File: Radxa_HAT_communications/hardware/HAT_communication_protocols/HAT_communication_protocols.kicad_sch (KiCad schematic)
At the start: 66 parts, among them J1 Conn_01x02_Pin, J2 Can_terminals, J3 120Can-resistor, J4 Power_supply_12V, J5 LoRa_DIO, Q1 NMOS, U1 AMS1117-5.0, U2 LD1117V33, U3 74HC04, U4 MAX3485, U5 MCP2515-xSO, U6 TJA1051T-3, Y1 8MHz

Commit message: new docummentation
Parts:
- removed C1: 100nf, symbol Device:C_Small
- removed C15: 100nf, Resistor_SMD:R_0603_1608Metric_Pad0.98x0.95mm_HandSolder, symbol Device:C_Small
- removed C3: x, symbol Device:C_Small
- removed L1: FerriteBead_0603_1.5A, 4ms_Resistor:R_0603, symbol PCM_4ms_Inductor:FerriteBead_0603_1.5A
- added C18: 1uf, Resistor_SMD:R_0603_1608Metric_Pad0.98x0.95mm_HandSolder, symbol Device:C_Small
- added C19: 10uf, Resistor_SMD:R_0603_1608Metric_Pad0.98x0.95mm_HandSolder, symbol Device:C_Small
- added C3: x, symbol Device:C_US
- added L1: L_Ferrite, symbol Device:L_Ferrite
- added U7: LD1117V33, Package_TO_SOT_SMD:SOT-223-3_TabPin2, symbol Regulator_Linear:LD1117V33
- 2-Pin_Power_input1: footprint 4ms_Connector:Pins_1x02_2.54mm_TH -> Connector_PinHeader_2.54mm:PinHeader_1x02_P2.54mm_Vertical
- C17, R4, R9: footprint (none) -> Resistor_SMD:R_0603_1608Metric_Pad0.98x0.95mm_HandSolder
- R2, R3: value 1K8 -> 2k4
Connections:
- net GPIO03 is gone; now on net CAN_SI: RadxaGPIO1.15 (Pin_15)
- net GPIO04 is gone; now on net CAN_SO: RadxaGPIO1.7 (Pin_7)
- net GPIO05 is gone; now on net CAN_CS: RadxaGPIO1.11 (Pin_11)
- net GPIO06 is gone; now on net CAN_SCK: RadxaGPIO1.13 (Pin_13)
- net RXD is gone; now on net GPIO21: U3.4, U3.5
- net TXD is gone; now on net GPIO20: R5.2, U3.1
- net 12V: now also C3.1, L1.2; no longer C4.1, C5.1, U1.3 (VI), U2.3 (VI)
- net GND: now also C18.2, C19.2, C3.2, U7.1 (GND)
- net PS+3.3v: no longer C16.1, SX1.13 (3.3V)
- net PS+5v: no longer U6.5 (VIO)
- net at D6.1 (A1), D7.2 (A2), F3.2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: now also R9.2
- net at D5.1 (A1), D6.2 (A2), F2.1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: now also J1.1 (Pin_1)
- net at C2.1, D10.1 (K), D3.2 (A2)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: now also L1.1
- net at F3.1, RS485_interface1.2 (Pin_2): no longer R9.2
- net at F2.2, RS485_interface1.1 (Pin_1): no longer J1.1 (Pin_1)
- new net: C4.1, U2.3 (VI)
- new net: C19.1, U7.3 (VI)
- new net: C5.1, U1.3 (VI)
- new net LoRa+3.3v: C16.1, C18.1, SX1.13 (3.3V), U7.2 (VO)
- no-connect marks 6 -> 7
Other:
- note added: "2.2mA MAX"
- note added: "80mA MAX"
- note added: "Transmit (TX) Current: 650 mA (maximum, at 30 dBm output power)"
- moved on the sheet: 2-Pin_Power_input1, C10, C11, C12, C13, C14, C17, C2, C4, C5, C6, C7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

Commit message: PCB design | PCB countors finally drew and correct placement of pinheaders and pin socker so they fit to the Radxa-X4 form factor
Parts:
- added J6: PoE, Connector_PinSocket_2.54mm:PinSocket_2x02_P2.54mm_Vertical, symbol Connector_Generic:Conn_02x02_Top_Bottom
- 2-Pin_Power_input1: footprint Connector_PinHeader_2.54mm:PinHeader_1x02_P2.54mm_Vertical -> Connector_PinSocket_2.54mm:PinSocket_1x02_P2.54mm_Vertical
- J2, J4: footprint TerminalBlock:TerminalBlock_Xinya_XY308-2.54-2P_1x02_P2.54mm_Horizontal -> TerminalBlock_MetzConnect:TerminalBlock_MetzConnect_Type101_RT01602HBWC_1x02_P5.08mm_Horizontal
- RS485_interface1: footprint TerminalBlock:TerminalBlock_Xinya_XY308-2.54-3P_1x03_P2.54mm_Horizontal -> TerminalBlock_CUI:TerminalBlock_CUI_TB007-508-03_1x03_P5.08mm_Horizontal
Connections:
- new net vc1: J6.2 (Pin_2)
- new net vc2: J6.1 (Pin_1)
- new net vc3: J6.4 (Pin_4)
- new net vc4: J6.3 (Pin_3)
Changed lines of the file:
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@@
 	(wire
 		(pts
+			(xy 388.62 102.87) (xy 387.35 102.87)
+		)
+		(stroke
+			(width 0)
+			(type default)
+		)
+	)
+	(wire
+		(pts
 			(xy 78.74 54.61) (xy 78.74 62.23)
 		)
@@
 	(wire
 		(pts
+			(xy 388.62 100.33) (xy 387.35 100.33)
+		)
+		(stroke
+			(width 0)
+			(type default)
+		)
+	)
+	(wire
+		(pts
 			(xy 215.9 152.4) (xy 213.36 152.4)
 		)
@@
 	(wire
 		(pts
+			(xy 402.59 102.87) (xy 401.32 102.87)
+		)
+		(stroke
+			(width 0)
+			(type default)
+		)
+	)
+	(wire
+		(pts
 			(xy 146.05 154.94) (xy 146.05 147.32)
 		)
@@
 	(wire
 		(pts
+			(xy 402.59 100.33) (xy 401.32 100.33)
+		)
+		(stroke
+			(width 0)
+			(type default)
+		)
+	)
+	(wire
+		(pts
 			(xy 125.73 124.46) (xy 125.73 127)
 		)
@@
 		)
 	)
+	(label "vc4"
+		(at 402.59 100.33 0)
+		(effects
+			(font
+				(size 1.27 1.27)
+			)
+			(justify left bottom)
+		)
+	)
 	(label "GPIO25"
 		(at 215.9 175.26 0)
@@
 		)
 	)
+	(label "vc1"
+		(at 387.35 102.87 180)
+		(effects
+			(font
+				(size 1.27 1.27)
+			)
+			(justify right bottom)
+		)
+	)
 	(label "GPIO06"
 		(at 304.8 152.4 0)
@@
 		)
 	)
+	(label "vc2"
+		(at 387.35 100.33 180)
+		(effects
+			(font
+				(size 1.27 1.27)
+			)
+			(justify right bottom)
+		)
+	)
 	(label "LoRa_D1"
 		(at 224.79 33.02 0)
@@
 		)
 	)
+	(label "vc3"
+		(at 402.59 102.87 0)
+		(effects
+			(font
+				(size 1.27 1.27)
+			)
+			(justify left bottom)
+		)
+	)
 	(label "GPIO03"
 		(at 198.12 144.78 180)
@@
 			)
 		)
-		(property "Footprint" "Connector_PinHeader_2.54mm:PinHeader_1x02_P2.54mm_Vertical"
+		(property "Footprint" "Connector_PinSocket_2.54mm:PinSocket_1x02_P2.54mm_Vertical"
 			(at 396.875 23.495 0)
 			(effects
@@
 	)
 	(symbol
+		(lib_id "Connector_Generic:Conn_02x02_Top_Bottom")
+		(at 393.7 100.33 0)
+		(unit 1)
+		(exclude_from_sim no)
+		(in_bom yes)
+		(on_board yes)
+		(dnp no)
+		(property "Reference" "J6"
+			(at 394.97 93.98 0)
+			(effects
+				(font
+					(size 1.27 1.27)
+				)
+			)
+		)
+		(property "Value" "PoE"
+			(at 394.97 96.52 0)
+			(effects
+				(font
+					(size 1.27 1.27)
+				)
+			)
+		)
+		(property "Footprint" "Connector_PinSocket_2.54mm:PinSocket_2x02_P2.54mm_Vertical"
+			(at 393.7 100.33 0)
+			(effects
+				(font
+					(size 1.27 1.27)
+				)
+				(hide yes)
+			)
+		)
+		(property "Datasheet" "~"
+			(at 393.7 100.33 0)
+			(effects
+				(font
+					(size 1.27 1.27)
+				)
+				(hide yes)
+			)
+		)
+		(property "Description" "Generic connector, double row, 02x02, top/bottom pin numbering scheme (row 1: 1...pins_per_row, row2: pins_per_row+1 ... num_pins), script generated (kicad-library-utils/schlib/autogen/connector/)"
+			(at 393.7 100.33 0)
+			(effects
+				(font
+					(size 1.27 1.27)
+				)
+				(hide yes)
+			)
+		)
+		(pin "2"
+		)
+		(pin "4"
+		)
+		(pin "1"
+		)
+		(pin "3"
+		)
+		(instances
+			(project ""
+				(path "/c2c24d05-340c-4010-9daf-2c9fe65e9278"
+					(reference "J6")
+					(unit 1)
+				)
+			)
+		)
+	)
+	(symbol
 		(lib_id "power:GND")
 		(at 78.74 76.2 0)
@@
 			)
 		)
-		(property "Footprint" "TerminalBlock:TerminalBlock_Xinya_XY308-2.54-2P_1x02_P2.54mm_Horizontal"
+		(property "Footprint" "TerminalBlock_MetzConnect:TerminalBlock_MetzConnect_Type101_RT01602HBWC_1x02_P5.08mm_Horizontal"
 			(at 304.8 30.48 0)
 			(effects
@@
 			)
 		)
-		(property "Footprint" "TerminalBlock:TerminalBlock_Xinya_XY308-2.54-2P_1x02_P2.54mm_Horizontal"
+		(property "Footprint" "TerminalBlock_MetzConnect:TerminalBlock_MetzConnect_Type101_RT01602HBWC_1x02_P5.08mm_Horizontal"
 			(at 154.94 134.62 0)
 			(effects
@@
 			)
 		)
-		(property "Footprint" "TerminalBlock:TerminalBlock_Xinya_XY308-2.54-3P_1x03_P2.54mm_Horizontal"
+		(property "Footprint" "TerminalBlock_CUI:TerminalBlock_CUI_TB007-508-03_1x03_P5.08mm_Horizontal"
 			(at 152.4 35.56 0)
 			(effects

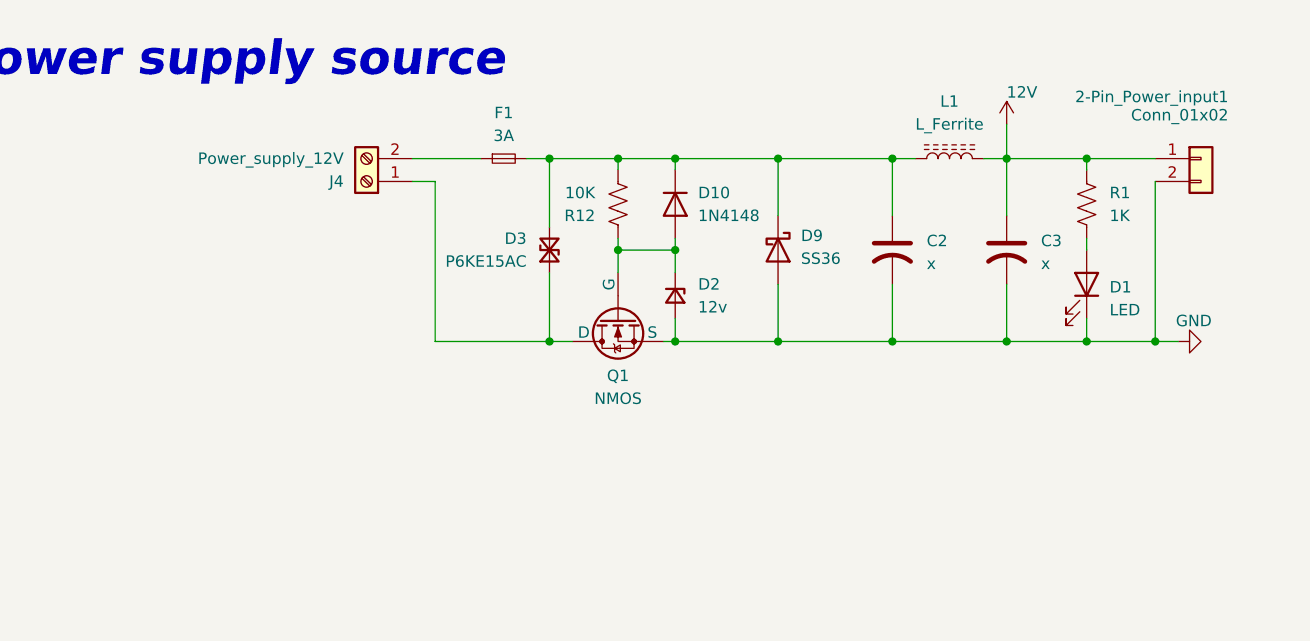
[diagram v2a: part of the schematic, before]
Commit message: Placement of some components in PCB layout. Thinking on adding a buck converter
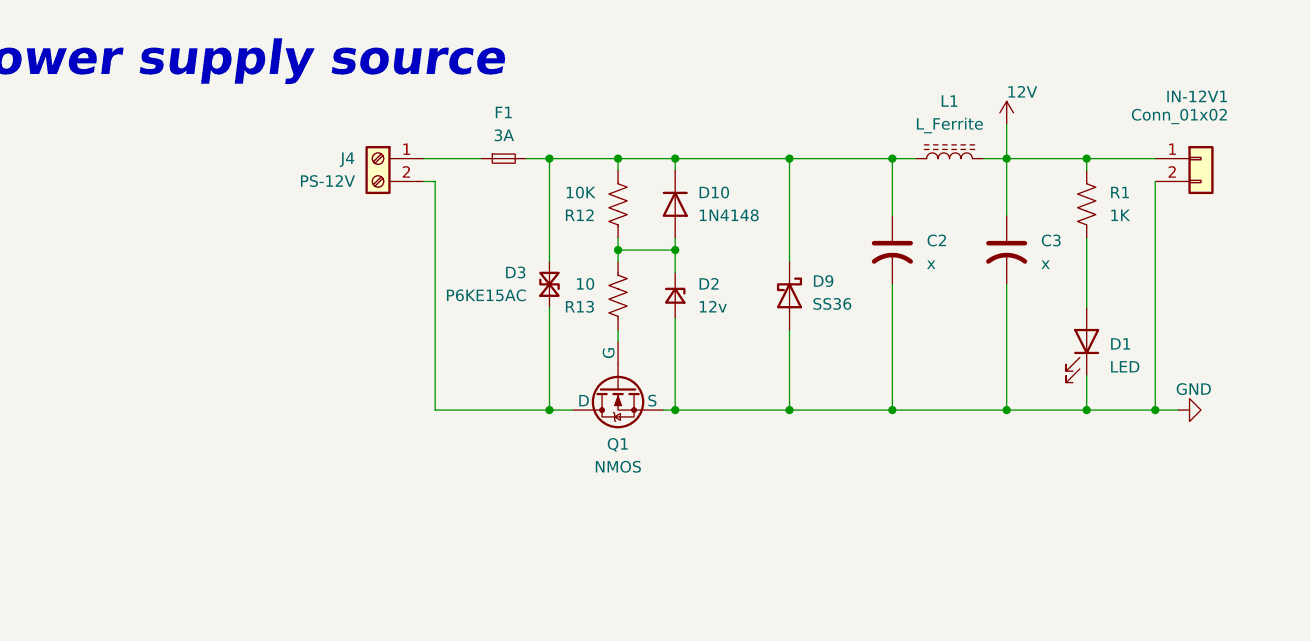
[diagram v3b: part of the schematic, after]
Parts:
- added R13: 10, Resistor_SMD:R_0603_1608Metric_Pad0.98x0.95mm_HandSolder, symbol Device:R_US
- J4: value Power_supply_12V -> PS-12V
- RS485_interface1: footprint TerminalBlock_CUI:TerminalBlock_CUI_TB007-508-03_1x03_P5.08mm_Horizontal -> TerminalBlock_MetzConnect:TerminalBlock_MetzConnect_Type101_RT01603HBWC_1x03_P5.08mm_Horizontal
- renumbered 2-Pin_Power_input1 to IN-12V1
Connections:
- net at D10.2 (A), D2.1 (K), R12.1: now also R13.2; no longer Q1.1 (G)
- net at F1.1: now also J4.1 (Pin_1); no longer J4.2 (Pin_2)
- net at D3.1 (A1), Q1.2 (D): now also J4.2 (Pin_2); no longer J4.1 (Pin_1)
- new net: Q1.1 (G), R13.1
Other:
- moved on the sheet: D1, D3, D9, J4, Q1

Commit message: PCB layout first version done
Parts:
- removed C2, C3: x, symbol Device:C_US
- removed D10: 1N4148, Diode_THT:D_DO-35_SOD27_P7.62mm_Horizontal, symbol Diode:1N4148
- removed L1: L_Ferrite, symbol Device:L_Ferrite
- removed U2: LD1117V33, Package_TO_SOT_SMD:SOT-223-3_TabPin2, symbol Regulator_Linear:LD1117V33
- added C1: 10uF /25v, Capacitor_SMD:C_1206_3216Metric_Pad1.33x1.80mm_HandSolder, symbol Device:C_US
- added C15: 10nf, Resistor_SMD:R_0603_1608Metric_Pad0.98x0.95mm_HandSolder, symbol Device:C_Small
- added C3: 22uF 6.3v, Capacitor_SMD:C_1206_3216Metric_Pad1.33x1.80mm_HandSolder, symbol Device:C_Small
- added D8: 1N4148W, Diode_SMD:D_SOD-123, symbol Diode:1N4148W
- added L2: 100uH_1.0A, Inductor_SMD:L_Wuerth_WE-PD-Typ-M-Typ-S_Handsoldering, symbol PCM_4ms_Inductor:10uH_1.0A_4018
- added R14: 100K, Resistor_SMD:R_0603_1608Metric_Pad0.98x0.95mm_HandSolder, symbol Device:R_US
- added R15: 6k8, Resistor_SMD:R_0603_1608Metric_Pad0.98x0.95mm_HandSolder, symbol Device:R_US
- added R16, R17: 10k, Resistor_SMD:R_0603_1608Metric_Pad0.98x0.95mm_HandSolder, symbol Device:R_US
- added U2: MP2307, Package_SO:SOIC-8-1EP_3.9x4.9mm_P1.27mm_EP2.62x3.51mm, symbol Regulator_Switching:MP2303ADN
- AE1: footprint (none) -> Connector_PinHeader_2.54mm:PinHeader_1x01_P2.54mm_Vertical
- C4: value 10uf -> 100nf
- C7: value 1uf -> 3.9nf
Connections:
- net LoRa+3.3v is gone; now on net PS+3.3v: C16.1, C18.1, SX1.13 (3.3V), U7.2 (VO)
- net 12V: now also D3.2 (A2), D9.1 (K), F1.2, R12.2, C1.1, D8.1 (K), R14.1, U2.2 (IN); no longer R1.1
- net COMs: now also RS485_interface1.1 (Pin_1); no longer RS485_interface1.3 (Pin_3)
- net GND: now also C1.2, C3.2, R15.2, R16.2, U2.4 (GND); no longer C7.2
- net PS+3.3v: no longer C7.1
- net PS+5v: now also C19.1, U7.3 (VI)
- net at R10.1, U6.6 (CANL): now also J2.1 (Pin_1); no longer J2.2 (Pin_2)
- net at J3.2 (Pin_2), U6.7 (CANH): now also J2.2 (Pin_2); no longer J2.1 (Pin_1)
- net at D2.1 (K), R12.1, R13.2: now also D8.2 (A)
- net at C4.1: now also U2.8 (SS)
- net at F2.2: now also RS485_interface1.3 (Pin_3); no longer RS485_interface1.1 (Pin_1)
- net PS+6.2v: now reaches C5.1, U1.3 (VI)
- net PS+6.2v: now also R1.1, C3.1, L2.2, R17.1
- new net: C7.2, R15.1
- new net: C7.1, U2.6 (COMP)
- new net: C15.2, L2.1, U2.3 (SW)
- new net: R16.1, R17.2, U2.5 (FB)
- new net: C15.1, U2.1 (BS)
- new net: R14.2, U2.7 (EN)
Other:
- note added: "Transmit (TX) Current: 120 mA (maximum, at +20 dBm output power)"
- note removed: "2.2mA MAX"
- note removed: "80mA MAX"
- note removed: "Transmit (TX) Current: 650 mA (maximum, at 30 dBm output power)"
- moved on the sheet: C8, D1, D2, D3, D9, F1, IN-12V1, J4, J6, Q1, R1, R12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

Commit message: PCB tracks 60% completed
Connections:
- net LoRa_D1: now also J5.3 (Pin_3); no longer J5.2 (Pin_2)
- net LoRa_D2: now also J5.2 (Pin_2); no longer J5.3 (Pin_3)
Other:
- moved on the sheet: C4
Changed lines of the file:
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@@
 	(wire
 		(pts
-			(xy 321.31 48.26) (xy 321.31 43.18)
+			(xy 321.31 53.34) (xy 321.31 43.18)
 		)
 		(stroke
@@
 	(wire
 		(pts
-			(xy 321.31 53.34) (xy 321.31 68.58)
+			(xy 321.31 58.42) (xy 321.31 68.58)
 		)
 		(stroke
@@
 	)
 	(image
-		(at 292.1 -26.67)
+		(at 342.9 -25.4)
 		(data "iVBORw0KGgoAAAANSUhEUgAAAyAAAAMgCAIAAABUEpE/AAAAA3NCSVQICAjb4U/gAAAgAElEQVR4"
 			"nOzdeZhU5Zk+/vfstXdVV1V3NU0D3SwiioBEdllkJCqCgtGYqKMmZtG4JJNkdDT5GicuuIwRiSYO"
@@
 		)
 	)
-	(label "LoRa_D2"
-		(at 233.68 90.17 180)
-		(effects
-			(font
-				(size 1.27 1.27)
-			)
-			(justify right bottom)
-		)
-	)
 	(label "SPI0_Tx"
 		(at 266.7 137.16 0)
@@
 		)
 	)
+	(label "LoRa_D2"
+		(at 233.68 92.71 180)
+		(effects
+			(font
+				(size 1.27 1.27)
+			)
+			(justify right bottom)
+		)
+	)
 	(label "COMs"
 		(at 116.84 60.96 0)
@@
 		)
 	)
-	(label "LoRa_D1"
-		(at 233.68 92.71 180)
-		(effects
-			(font
-				(size 1.27 1.27)
-			)
-			(justify right bottom)
-		)
-	)
 	(label "SPI0_NSS"
 		(at 304.8 143.51 0)
@@
 		)
 	)
+	(label "LoRa_D1"
+		(at 233.68 90.17 180)
+		(effects
+			(font
+				(size 1.27 1.27)
+			)
+			(justify right bottom)
+		)
+	)
 	(label "GPIO26"
 		(at 215.9 170.18 0)
@@
 		(lib_id "Device:C_Small")
 		(at 330.2 55.88 0)
-		(mirror y)
 		(unit 1)
 		(exclude_from_sim no)
@@
 		(dnp no)
 		(property "Reference" "C7"
-			(at 332.74 55.88 0)
+			(at 327.66 55.88 0)
 			(effects
 				(font
@@
 		)
 		(property "Value" "3.9nf"
-			(at 332.74 53.34 0)
+			(at 327.66 53.34 0)
 			(effects
 				(font
@@
 		(dnp no)
 		(property "Reference" "J6"
-			(at 307.848 86.36 0)
+			(at 309.88 86.36 0)
 			(effects
 				(font
@@
 		)
 		(property "Value" "PoE"
-			(at 311.15 86.36 0)
+			(at 313.182 86.36 0)
 			(effects
 				(font
@@
 	(symbol
 		(lib_id "Device:C_Small")
-		(at 321.31 50.8 0)
-		(mirror y)
+		(at 321.31 55.88 0)
 		(unit 1)
 		(exclude_from_sim no)
@@
 		(dnp no)
 		(property "Reference" "C4"
-			(at 323.85 50.8 0)
+			(at 318.77 55.88 0)
 			(effects
 				(font
@@
 		)
 		(property "Value" "100nf"
-			(at 323.85 48.26 0)
+			(at 318.77 53.34 0)
 			(effects
 				(font
@@
 		)
 		(property "Footprint" "Resistor_SMD:R_0603_1608Metric_Pad0.98x0.95mm_HandSolder"
-			(at 321.31 50.8 0)
+			(at 321.31 55.88 0)
 			(effects
 				(font
@@
 		)
 		(property "Datasheet" "~"
-			(at 321.31 50.8 0)
+			(at 321.31 55.88 0)
 			(effects
 				(font
@@
 		)
 		(property "Description" "Unpolarized capacitor, small symbol"
-			(at 321.31 50.8 0)
+			(at 321.31 55.88 0)
 			(effects
 				(font

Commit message: PCB V1 done
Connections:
- net 3.3v_gpio renamed 3.3v_pin1
- net 3.3v_pin1: no longer RadxaGPIO1.17 (Pin_17)
- net 5v_gpio renamed 5v_pin2
- net 5v_pin2: no longer RadxaGPIO1.4 (Pin_4)
- new net 3.3v_pin17: RadxaGPIO1.17 (Pin_17)
- new net 5v_pin4: RadxaGPIO1.4 (Pin_4)
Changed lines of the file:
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@@
 	)
 	(junction
-		(at 214.63 127)
-		(diameter 0)
-		(color 0 0 0 0)
-	)
-	(junction
 		(at 34.29 151.13)
 		(diameter 0)
@@
 	(wire
 		(pts
-			(xy 213.36 129.54) (xy 214.63 129.54)
+			(xy 213.36 129.54) (xy 222.25 129.54)
 		)
 		(stroke
@@
 	(wire
 		(pts
-			(xy 222.25 127) (xy 214.63 127)
-		)
-		(stroke
-			(width 0)
-			(type default)
-		)
-	)
-	(wire
-		(pts
 			(xy 21.59 52.07) (xy 21.59 55.88)
 		)
@@
 	(wire
 		(pts
-			(xy 214.63 129.54) (xy 214.63 127)
-		)
-		(stroke
-			(width 0)
-			(type default)
-		)
-	)
-	(wire
-		(pts
 			(xy 215.9 165.1) (xy 213.36 165.1)
 		)
@@
 	(wire
 		(pts
-			(xy 214.63 127) (xy 213.36 127)
-		)
-		(stroke
-			(width 0)
-			(type default)
-		)
-	)
-	(wire
-		(pts
 			(xy 236.22 44.45) (xy 236.22 45.72)
 		)
@@
 	(wire
 		(pts
+			(xy 213.36 127) (xy 222.25 127)
+		)
+		(stroke
+			(width 0)
+			(type default)
+		)
+	)
+	(wire
+		(pts
 			(xy 365.76 48.26) (xy 363.22 48.26)
 		)
@@
 			)
 		)
-		(property "Value" "5v_gpio"
+		(property "Value" "5v_pin2"
 			(at 225.552 127 90)
 			(effects
@@
 		(lib_id "Device:R_US")
 		(at 106.68 27.94 0)
+		(mirror y)
 		(unit 1)
 		(exclude_from_sim no)
@@
 		(dnp no)
 		(property "Reference" "R7"
-			(at 109.22 26.6699 0)
+			(at 104.14 26.6699 0)
 			(effects
 				(font
@@
 		)
 		(property "Value" "4K7"
-			(at 109.22 29.2099 0)
+			(at 104.14 29.2099 0)
 			(effects
 				(font
@@
 		)
 		(property "Footprint" "Resistor_SMD:R_0603_1608Metric_Pad0.98x0.95mm_HandSolder"
-			(at 107.696 28.194 90)
+			(at 105.664 28.194 90)
 			(effects
 				(font
@@
 			)
 		)
-		(property "Value" "3.3v_gpio"
+		(property "Value" "3.3v_pin17"
 			(at 182.626 147.066 90)
 			(effects
@@
 	)
 	(symbol
+		(lib_id "power:VCC")
+		(at 222.25 129.54 270)
+		(unit 1)
+		(exclude_from_sim no)
+		(in_bom yes)
+		(on_board yes)
+		(dnp no)
+		(property "Reference" "#PWR046"
+			(at 218.44 129.54 0)
+			(effects
+				(font
+					(size 1.27 1.27)
+				)
+				(hide yes)
+			)
+		)
+		(property "Value" "5v_pin4"
+			(at 225.552 129.54 90)
+			(effects
+				(font
+					(size 1.27 1.27)
+				)
+				(justify left)
+			)
+		)
+		(property "Footprint" ""
+			(at 222.25 129.54 0)
+			(effects
+				(font
+					(size 1.27 1.27)
+				)
+				(hide yes)
+			)
+		)
+		(property "Datasheet" ""
+			(at 222.25 129.54 0)
+			(effects
+				(font
+					(size 1.27 1.27)
+				)
+				(hide yes)
+			)
+		)
+		(property "Description" "Power symbol creates a global label with name \"VCC\""
+			(at 222.25 129.54 0)
+			(effects
+				(font
+					(size 1.27 1.27)
+				)
+				(hide yes)
+			)
+		)
+		(pin "1"
+		)
+		(instances
+			(project "HAT_communication_protocols"
+				(path "/c2c24d05-340c-4010-9daf-2c9fe65e9278"
+					(reference "#PWR046")
+					(unit 1)
+				)
+			)
+		)
+	)
+	(symbol
 		(lib_id "Device:D_Zener_Small")
 		(at 288.29 54.61 270)
@@
 			)
 		)
-		(property "Value" "3.3v_gpio"
+		(property "Value" "3.3v_pin1"
 			(at 182.88 127 90)
 			(effects

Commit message: PCB V1.3 done
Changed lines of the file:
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@@
+	)
+	(symbol
+		(lib_id "Graphic:Logo_Open_Hardware_Small")
+		(at 400.05 261.62 0)
+		(unit 1)
+		(exclude_from_sim no)
+		(in_bom no)
+		(on_board no)
+		(dnp no)
+		(fields_autoplaced yes)
+		(property "Reference" "#SYM1"
+			(at 400.05 254.635 0)
+			(effects
+				(font
+					(size 1.27 1.27)
+				)
+				(hide yes)
+			)
+		)
+		(property "Value" "Logo_Open_Hardware_Small"
+			(at 400.05 267.335 0)
+			(effects
+				(font
+					(size 1.27 1.27)
+				)
+				(hide yes)
+			)
+		)
+		(property "Footprint" ""
+			(at 400.05 261.62 0)
+			(effects
+				(font
+					(size 1.27 1.27)
+				)
+				(hide yes)
+			)
+		)
+		(property "Datasheet" "~"
+			(at 400.05 261.62 0)
+			(effects
+				(font
+					(size 1.27 1.27)
+				)
+				(hide yes)
+			)
+		)
+		(property "Description" "Open Hardware logo, small"
+			(at 400.05 261.62 0)
+			(effects
+				(font
+					(size 1.27 1.27)
+				)
+				(hide yes)
+			)
+		)
+		(property "Sim.Enable" "0"
+			(at 400.05 261.62 0)
+			(effects
+				(font
+					(size 1.27 1.27)
+				)
+				(hide yes)
+			)
+		)
+		(instances
+			(project ""
+				(path "/c2c24d05-340c-4010-9daf-2c9fe65e9278"
+					(reference "#SYM1")
+					(unit 1)
+				)
+			)
+		)
 	)
 	(symbol

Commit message: PCB V1.4 done
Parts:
- added TP1, TP2, TP3, TP4, TP5: TestPoint_Probe, TestPoint:TestPoint_Pad_D1.0mm, symbol Connector:TestPoint_Probe
- renumbered C14 to C1, C5 to C10, C19 to C11, C18 to C12, C16 to C13, C1 to C14, C4 to C15, C7 to C16, C15 to C17, C3 to C18, C13 to C2, C11 to C3, C10 to C4, C9 to C5, C17 to C6, C12 to C7, C6 to C9, D4 to D1, D5 to D2, D6 to D3, D7 to D4, D3 to D5, D8 to D6, D2 to D7, D9 to D8, D1 to D9, F2 to F1, F3 to F2, F1 to F3, J5 to J4, J4 to J5, L2 to L1, R5 to R1, R12 to R11, R13 to R12, R14 to R13, R15 to R14, R16 to R15, R17 to R16, R1 to R17, R6 to R5, R11 to R6, RadxaGPIO1 to Radxa-IO1, U3 to U1, U5 to U2, U4 to U3, U6 to U4, U1 to U5, U7 to U6, U2 to U7
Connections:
- net GPIO07 is gone; now on net CAN_INT: Radxa-IO1.29 (Pin_29)
- net LoRa_RST is gone; now on net GPIO11: SX1.6 (RESET)
- net 12V: now also TP4.1
- net PS+3.3v: now also TP2.1, TP3.1
- net PS+5v: now also TP1.1
- net PS+6.2v: now also TP5.1
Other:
- moved on the sheet: J4
